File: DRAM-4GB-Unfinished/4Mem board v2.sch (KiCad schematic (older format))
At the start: 29 parts, among them P1 CONN_1, P11 CONN_2X2, P2 CONN_1, P3 CONN_1, P4 CONN_1, P8 CONN_20X2, P9 CONN_20X2, U1 XC6SLX45-2FGG484C, U2 DDR3_DIMM_240PIN, U7 LM1086CS_TO252_DPAK

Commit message: DRAM-4GB-Unfinished: wire DDR3 DIMM address, data and strobes to the FPGA
Source: S100 4GB DRAM BOARD/4Mem board v2/backups/03-05-2015 2323
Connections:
- net labels added: DDR3_A0, DDR3_A1, DDR3_A10, DDR3_A11, DDR3_A12, DDR3_A13, DDR3_A14, DDR3_A15, DDR3_A2, DDR3_A3, DDR3_A4, DDR3_A5, DDR3_A6, DDR3_A7, DDR3_A8, DDR3_A9, DDR3_BA0, DDR3_BA1, DDR3_BA2, DDR3_CAS, DDR3_CK0h, DDR3_CK0l, DDR3_CK1h, DDR3_CK1l, DDR3_CKE0, DDR3_CKE1, DDR3_DM0, DDR3_DM1, DDR3_DM2, DDR3_DM3, DDR3_DM4, DDR3_DM5, DDR3_DM6, DDR3_DM7, DDR3_DQ0, DDR3_DQ1, DDR3_DQ10, DDR3_DQ11, DDR3_DQ12, DDR3_DQ13, DDR3_DQ14, DDR3_DQ15, DDR3_DQ16, DDR3_DQ17, DDR3_DQ18, DDR3_DQ19, DDR3_DQ2, DDR3_DQ20, DDR3_DQ21, DDR3_DQ22, DDR3_DQ23, DDR3_DQ24, DDR3_DQ25, DDR3_DQ26, DDR3_DQ27, DDR3_DQ28, DDR3_DQ29, DDR3_DQ3, DDR3_DQ30, DDR3_DQ31, DDR3_DQ32, DDR3_DQ33, DDR3_DQ34, DDR3_DQ35, DDR3_DQ36, DDR3_DQ37, DDR3_DQ38, DDR3_DQ39, DDR3_DQ4, DDR3_DQ40, DDR3_DQ41, DDR3_DQ42, DDR3_DQ43, DDR3_DQ44, DDR3_DQ45, DDR3_DQ46, DDR3_DQ47, DDR3_DQ48, DDR3_DQ49, DDR3_DQ5, DDR3_DQ50, DDR3_DQ51, DDR3_DQ52, DDR3_DQ53, DDR3_DQ54, DDR3_DQ55, DDR3_DQ56, DDR3_DQ57, DDR3_DQ58, DDR3_DQ59, DDR3_DQ6, DDR3_DQ60, DDR3_DQ61, DDR3_DQ62, DDR3_DQ63, DDR3_DQ7, DDR3_DQ8, DDR3_DQ9, DDR3_DQS0h, DDR3_DQS0l, DDR3_DQS1h, DDR3_DQS1l, DDR3_DQS2h, DDR3_DQS2l, DDR3_DQS3h, DDR3_DQS3l, DDR3_DQS4h, DDR3_DQS4l, DDR3_DQS5h, DDR3_DQS5l, DDR3_DQS6h, DDR3_DQS6l, DDR3_DQS7h, DDR3_DQS7l, DDR3_ODT0, DDR3_OFT1, DDR3_RAS, DDR3_S0l, DDR3_S1l, DDR3_WE
- wire segments 356 -> 600
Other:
- moved on the sheet: U2D, U2E

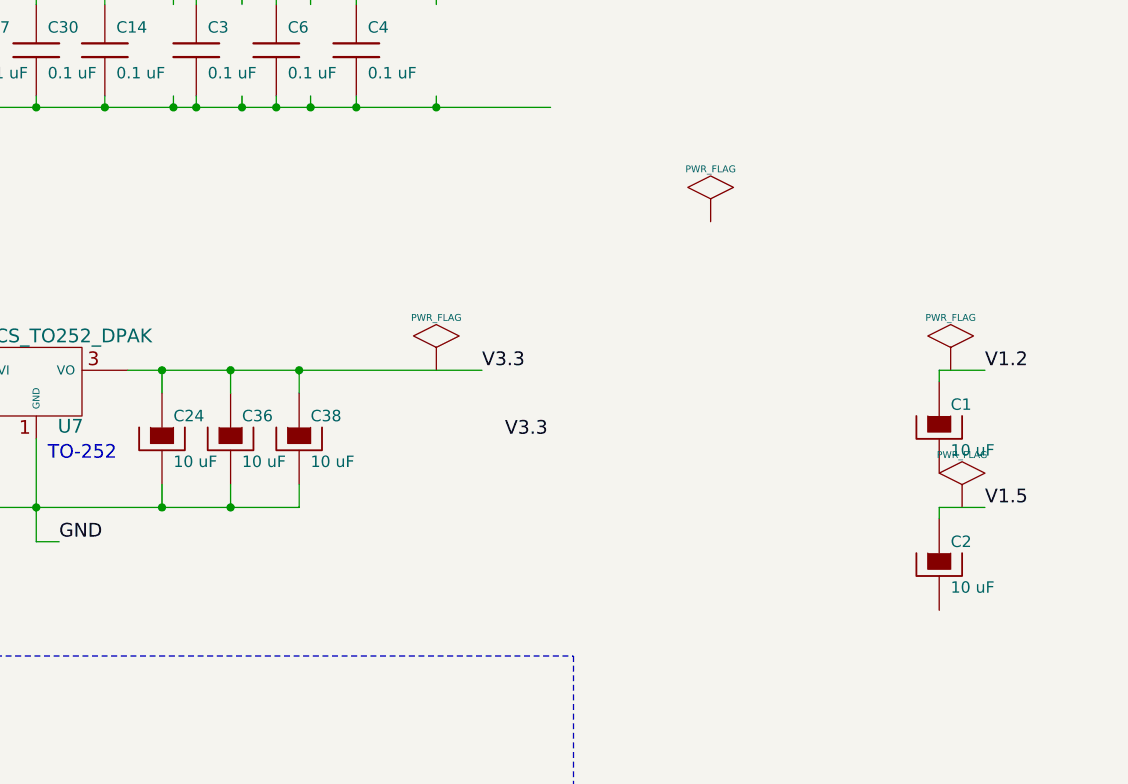
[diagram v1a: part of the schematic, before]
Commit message: DRAM-4GB-Unfinished: annotate power flags
Source: S100 4GB DRAM BOARD/4Mem board v2/backups/04-05-2015 0939 (04-05-2015 1910 is byte-identical and is skipped; _autosave file left out)
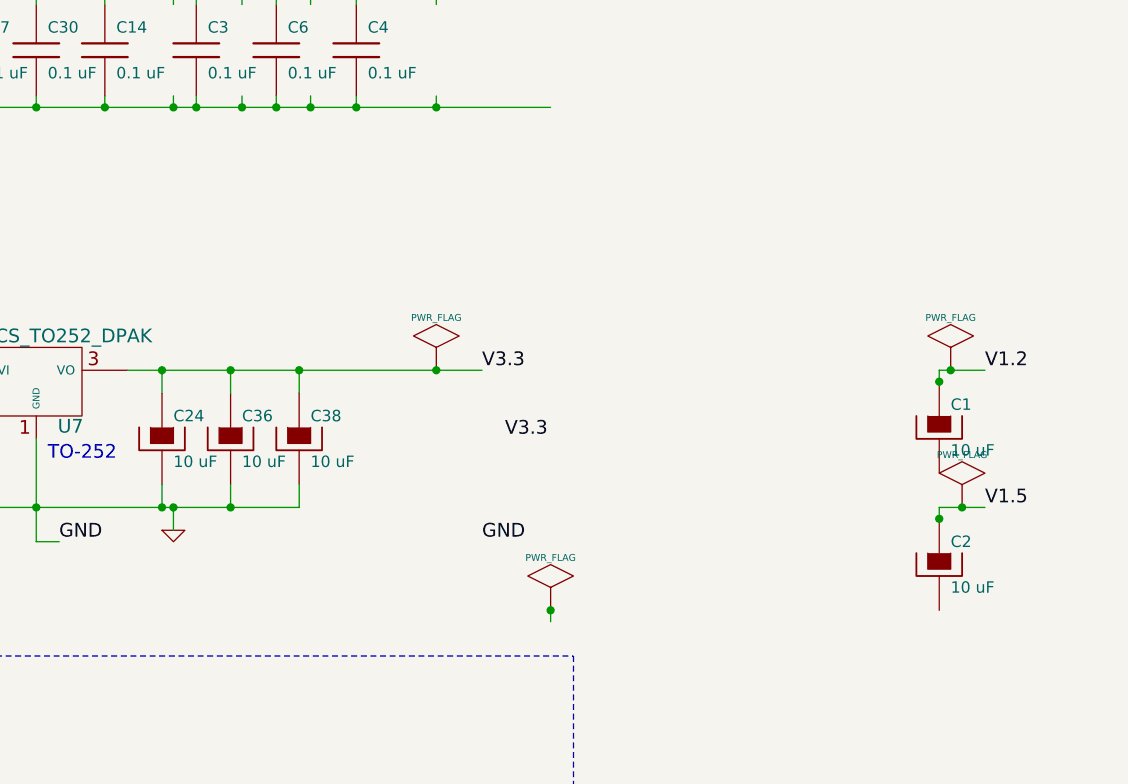
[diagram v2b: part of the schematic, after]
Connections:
- wire segments 600 -> 602
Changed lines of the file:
@@
 Connection ~ 36450 21350
 $Comp
-L PWR_FLAG #FLG?
-U 1 1 554AB1BD
-P 4800 13850
-F 0 "#FLG?" H 4800 14120 30  0001 C CNN
-F 1 "PWR_FLAG" H 4800 14080 30  0000 C CNN
-F 2 "" H 4800 13850 60  0001 C CNN
-F 3 "" H 4800 13850 60  0001 C CNN
-	1    4800 13850
-	1    0    0    -1
-$EndComp
-$Comp
-L PWR_FLAG #FLG?
+L PWR_FLAG #FLG05
 U 1 1 554AB1C4
 P 3600 14500
-F 0 "#FLG?" H 3600 14770 30  0001 C CNN
+F 0 "#FLG05" H 3600 14770 30  0001 C CNN
 F 1 "PWR_FLAG" H 3600 14730 30  0000 C CNN
 F 2 "" H 3600 14500 60  0001 C CNN
@@
 $EndComp
 $Comp
-L PWR_FLAG #FLG?
+L PWR_FLAG #FLG06
 U 1 1 554AB1CA
 P 5850 14500
-F 0 "#FLG?" H 5850 14770 30  0001 C CNN
+F 0 "#FLG06" H 5850 14770 30  0001 C CNN
 F 1 "PWR_FLAG" H 5850 14730 30  0000 C CNN
 F 2 "" H 5850 14500 60  0001 C CNN
@@
 $EndComp
 $Comp
-L PWR_FLAG #FLG?
+L PWR_FLAG #FLG07
 U 1 1 554AB1D0
 P 5900 15100
-F 0 "#FLG?" H 5900 15370 30  0001 C CNN
+F 0 "#FLG07" H 5900 15370 30  0001 C CNN
 F 1 "PWR_FLAG" H 5900 15330 30  0000 C CNN
 F 2 "" H 5900 15100 60  0001 C CNN
@@
 	1    0    0    -1
 $EndComp
+Text Label 3800 15250 0    60   ~ 0
+GND
+$Comp
+L GND #PWR08
+U 1 1 554ACAEB
+P 2450 15200
+F 0 "#PWR08" H 2450 15200 30  0001 C CNN
+F 1 "GND" H 2450 15130 30  0001 C CNN
+F 2 "" H 2450 15200 60  0001 C CNN
+F 3 "" H 2450 15200 60  0001 C CNN
+	1    2450 15200
+	1    0    0    -1
+$EndComp
+$Comp
+L PWR_FLAG #FLG09
+U 1 1 554ACAF1
+P 4100 15550
+F 0 "#FLG09" H 4100 15820 30  0001 C CNN
+F 1 "PWR_FLAG" H 4100 15780 30  0000 C CNN
+F 2 "" H 4100 15550 60  0001 C CNN
+F 3 "" H 4100 15550 60  0001 C CNN
+	1    4100 15550
+	1    0    0    -1
+$EndComp
+Connection ~ 4100 15550
+Wire Wire Line
+	4100 15550 4100 15600
+Wire Wire Line
+	2450 15100 2450 15200
+Connection ~ 2450 15100
+Connection ~ 3600 14500
+Connection ~ 5850 14500
+Connection ~ 5800 14550
+Connection ~ 5900 15100
+Connection ~ 5800 15150
 $EndSCHEMATC

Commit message: DRAM-4GB-Unfinished: add regulators, P8/P9 I/O nets, start BGA fanout
Source: S100 4GB DRAM BOARD/4Mem board v2/backups/09-05-2015 1716
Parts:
- removed C1, C2: 10 uF, symbol CP
- removed C3: 0.1 uF, C2, symbol C
- removed U7: LM1086CS_TO252_DPAK, ~, symbol LM1086CS_TO252_DPAK
- added C10, C11, C12, C13, C15, C16, C17, C19, C20, C21, C3, C5, C7, C8, C9: 10 uF, symbol CP
- added C22, C23, C25, C26, C28, C29, C31: 0.1 uF, C2, symbol C
- added D2: LED, symbol LED
- added Q1: ^^NPN-BC817-SOT323, symbol ^^NPN-BC817-SOT323
- added R10, R3, R4, R7, R9: 4K7, symbol R
- added R11, R2: 330, symbol R
- added R8: 0, symbol R
- added SW1: PROG_B, symbol SW_PUSH
- added U3: XCF08P-VO48/TSOP48, ~, symbol XCF08P-VO48/TSOP48
- added U4: LM1117MP-1.8, ~, symbol LM1117MP-1.8
- added U5: AZ1084, ~, symbol AZ1084
- added U6: NCP565, ~, symbol NCP565
- added U7: LT1764EQ-1.5, ~, symbol LT1764EQ-1.5
- added U8: RT9026_MSOP-10, symbol RT9026_MSOP-10
- C30: footprint (none) -> C2
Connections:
- net labels added: +8Vitemp, DDR3_VREF, DDR3_VTT, DONE_LED_SIGNAL, FPGA_CCLK_2, FPGA_CMPCS_B, FPGA_CSI_B, FPGA_DONE, FPGA_HSWAPEN, FPGA_INIT_B, FPGA_M0, FPGA_M1, FPGA_PROGRAM_B, FPGA_RDWR_B, FPGA_SUSPEND, FPGA_TDI, FPGA_TDO, IO_000, IO_001, IO_002, IO_003, IO_004, IO_005, IO_006, IO_007, IO_008, IO_009, IO_010, IO_011, IO_012, IO_013, IO_014, IO_015, IO_016, IO_017, IO_018, IO_019, IO_020, IO_021, IO_022, IO_023, IO_024, IO_025, IO_026, IO_027, IO_028, IO_029, IO_030, IO_031, IO_032, IO_033, IO_034, IO_035, IO_036, IO_037, IO_038, IO_039, IO_040, IO_041, IO_042, IO_043, IO_044, IO_045, IO_046, IO_047, IO_048, IO_049, IO_050, IO_051, IO_052, IO_053, IO_054, IO_055, IO_056, IO_057, IO_058, IO_059, IO_060, IO_061, IO_062, IO_063, IO_064, IO_065, IO_066, IO_067, IO_068, IO_069, IO_070, IO_071, IO_072, IO_073, IO_074, IO_075, IO_076, IO_077, IO_078, IO_079, IO_080, IO_081, IO_082, IO_083, IO_084, IO_085, IO_086, IO_087, IO_088, IO_089, IO_090, IO_091, IO_092, IO_093, IO_094, IO_095, IO_096, IO_097, IO_098, IO_099, IO_100, IO_101, IO_102, IO_103, IO_104, IO_105, IO_106, IO_107, IO_108, IO_109, PF_D0, PF_D1, PF_D2, PF_D3, PF_D4, PF_D5, PF_D6, PF_D7, PF_TDI, PF_TDO, V1.2temp, V1.5temp, V1.8, V3.3b, V3.3c, V3.3temp, mmPF_TDO, mm_TCK, mm_TMS
- net labels removed: mmCPLD1_TCK, mmCPLD1_TMS, mmFPGA_TDO
- wire segments 602 -> 912
- no-connect marks 25 -> 28
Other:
- note added: "1"
- note added: "1.2V"
- note added: "1.2V Fixed 1.5A , Vin 2.5 V-9 V\nTO-232-3\nDigi# NCP565D2T12GOS-ND"
- note added: "1.5V"
- note added: "1.5V Fixed 3A , Vin 2.7 V- 20 V\nTO-263-6, D²Pak (5 Leads + Tab), TO-263BA\nLT1764EQ-1.5#PBF-ND"
- note added: "1.8V"
- note added: "1.8V Fixed 800mA, up to 15 V\nSOT-223\nDigi# LM1117MP-1.8/NOPBCT-ND"
- note added: "2+tab"
- note added: "3"
- note added: "3.3V"
- note added: "3.3V Fixed 5A, 6.3 V- 12 V\nTO-232-3\nDigi# AZ1084CS2-3.3TRE1DICT-ND"
- note added: "D11\nC12\nA3\nA4\nD7\nD8\nB8\nA8\nD6\nC6\nC5\nA5\nB6\nA6\nC7\nA7"
- note added: "DONE_LED"
- note added: "FPGA pin\nD0 -> AA20\nD1 -> U14\nD2 -> U13\nD3 -> AA6\nD4 -> AB6\nD5 -> W4\nD6 -> Y4\nD7 -> Y7\n\nM0 -> AA22\nM1 -> U15\n\nHSWAPEN -> A3\nDONE_2 -> Y22\nCCLK -> Y21\nINIT_B -> T6\nCSI_B -> AB20\nCSO_B -> T5\nPROGRAM_B -> AA1\nRDWR_B -> AB7\n\nDOUT_BUSY -> T20\nSUSPEND -> N15\n\nTCK -> G15\nTDI -> E18\nTMS -> C18\nTDO -> A19"
- note added: "JTAG Chain"
- note added: "Leave unconnected or pull to VCCO_2"
- note added: "PROG_B"
- note added: "W12\nY12\nAA14\nAB14\nAA21\nAB21\nY19\nAB19\nU15\nV15\nY21\nAA22\nT6\nT5\nAA20\nAB20\n"
- note added: "XCF16P - VOG48"
- note added: "from Adapter board\n -> input to FPGA"
- note added: "output from PF -> into Adapter board\nfrom Adapter board -> input to FPGA"
- note added: "output from PF\n -> into Adapter board"
- note removed: "TO-252"
- moved on the sheet: C14, C18, C24, C27, C34, C36, C38, C4, C6, D1, P1, P2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

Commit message: DRAM-4GB-Unfinished: connect all P8/P9 signals to the FPGA; BGA power fanout
Source: S100 4GB DRAM BOARD/4Mem board v2/backups/23-05-2015 2046 (newest file is 2015-05-17)
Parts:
- added C1, C32, C33, C35, C37, C39, C40, C41, C42, C43: 0.1 uF, C2, symbol C
- added C2: 0.1 uF, symbol C
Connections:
- net labels added: V3.3temp2
- net labels removed: B0_CE*, B0_WE*, B1_CE*, B1_WE*, B2_CE*, B2_WE*, B3_CE*, B3_WE*, V3.3b
- wire segments 912 -> 1015
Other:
- note removed: "INPUT to CPLD"
- note removed: "OUTPUT FROM CPLD"

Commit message: DRAM-4GB-Unfinished: add PIC18F2520, XCF08P config flash and 2.5 V clock; last PCB edits; DigiKey parts list
Source: S100 4GB DRAM BOARD/4Mem board v2/(top level) (working folder; .dsn/.ses/.bak, BMP screenshots, datasheets and saved web pages left out)
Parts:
- added C44, C46, C47, C48: 10 uF, symbol CP
- added C45: 0.1 uF, C2, symbol C
- added P5: CONN_6X2, symbol CONN_6X2
- added R12, R13: 10K, symbol R
- added U10: LM1117MP-2.5, ~, symbol LM1117MP-1.8
- added U12: PIC18F2520-28QFN, symbol PIC18F2520-28QFN
- added U9: FPGA_CLK_0, symbol CRYSTAL_OSC_SMD
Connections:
- net labels added: DDR3_SCL, DDR3_SDA, FPGA_CLK_0, PIC_IO1, PIC_IO2, PIC_IO3, PIC_IO4, PIC_IO5, PIC_IO6, PIC_MCLR, PIC_PGC, PIC_PGD, PIC_PGM, PIC_RX, PIC_TX, V2.5
- wire segments 1015 -> 1087
- no-connect marks 28 -> 30
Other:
- note added: "2.5V"
- note added: "2.5V Fixed 1.5A, up to 15 Vin\nSOT-223\nDigi# LM1117MPX-2.5/NOPBCT-ND\nor ebay: AMS1117-2.5"
- note added: "FPGA DONE Signal:\nActive-High signal indicating configuration is\ncomplete:\n0 = FPGA not configured\n1 = FPGA configured"
- moved on the sheet: C22, C23, C25, C26, C28, C29, C30, C31, U8
